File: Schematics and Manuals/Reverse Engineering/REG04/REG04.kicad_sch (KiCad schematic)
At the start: 203 parts, among them J1 Conn_01x02_Pin, J10 Conn_01x02_Pin, J11 Conn_01x02_Pin, J12 Conn_01x02_Pin, J13 Conn_01x02_Pin, J14 Conn_01x02_Pin, J15 Conn_01x02_Pin, J16 Conn_01x02_Pin, J17 Conn_01x02_Pin, J18 Conn_01x02_Pin, J19 Conn_01x02_Pin, J2 Conn_01x02_Pin, J20 Conn_01x02_Pin, J21 Conn_01x02_Pin, J22 Conn_01x02_Pin, J23 Conn_01x02_Pin, J24 Conn_01x02_Pin, J25 Conn_01x02_Pin, J26 Conn_01x02_Pin, J27 Conn_01x02_Pin, J28 Conn_01x02_Pin, J29 Conn_01x02_Pin, J3 Conn_01x02_Pin, J30 Conn_01x02_Pin, J31 Conn_01x02_Pin, J32 Conn_01x02_Pin, J33 Conn_01x02_Pin, J34 Conn_01x02_Pin, J35 Conn_01x02_Pin, J36 Conn_01x02_Pin, J37 Conn_01x02_Pin, J38 Conn_01x02_Pin, J39 Conn_01x02_Pin, J4 Conn_01x02_Pin, J40 Conn_01x02_Pin, J5 Conn_01x02_Pin, J6 Conn_01x02_Pin, J7 Conn_01x02_Pin, J8 Conn_01x02_Pin, J9 Conn_01x02_Pin, Q1 Q_PNP_EBC, Q10 Q_PNP_EBC, Q11 Q_PNP_EBC, Q12 Q_PNP_EBC, Q13 Q_PNP_EBC, Q14 Q_PNP_EBC, Q15 Q_PNP_EBC, Q16 Q_PNP_EBC, Q2 Q_PNP_EBC, Q3 Q_PNP_EBC, Q4 Q_PNP_EBC, Q5 Q_PNP_EBC, Q6 Q_PNP_EBC, Q7 Q_PNP_EBC, Q8 Q_PNP_EBC, Q9 Q_PNP_EBC

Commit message: Complete renumbering and reordering of the schematic and PCB
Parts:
- R46: renamed from R31; value R -> 10k
- R61: renamed from R16; value R -> 10k
- renumbered C22 to C1, C14 to C10, C15 to C11, C9 to C13, C10 to C14, C11 to C15, C8 to C16, C5 to C17, C6 to C18, C7 to C19, C21 to C2, C4 to C20, C2 to C21, C3 to C22, C1 to C23, C18 to C3, C20 to C4, C17 to C5, C19 to C6, C23 to C7, C16 to C8, C13 to C9, D43 to D1, D35 to D10, D46 to D11, D34 to D12, D40 to D13, D33 to D14, D38 to D15, D39 to D16, D30 to D17, D31 to D18, D32 to D19, D48 to D2, D27 to D20, D28 to D21, D26 to D22, D29 to D23, D25 to D24, D22 to D25, D23 to D26, D24 to D27, D19 to D28, D20 to D29, D42 to D3, D21 to D30, D18 to D31, D17 to D32, D14 to D33, D15 to D34, D16 to D35, D11 to D36, D12 to D37, D13 to D38, D10 to D39, D45 to D4, D9 to D40, D7 to D41, D8 to D42, D6 to D43, D5 to D44, D3 to D45, D2 to D46, D4 to D47, D1 to D48, D37 to D5, D36 to D6, D44 to D7, D41 to D8, D47 to D9, J40 to J1, J31 to J10, J30 to J11, J29 to J12, J28 to J13, J27 to J14, J26 to J15, J25 to J16, J24 to J17, J23 to J18, J22 to J19, J39 to J2, J21 to J20, J20 to J21, J19 to J22, J18 to J23, J17 to J24, J16 to J25, J15 to J26, J14 to J27, J13 to J28, J12 to J29, J38 to J3, J11 to J30, J10 to J31, J9 to J32, J8 to J33, J7 to J34, J6 to J35, J5 to J36, J4 to J37, J3 to J38, J2 to J39, J37 to J4, J1 to J40, J36 to J5, J35 to J6, J34 to J7, J33 to J8, J32 to J9, Q14 to Q1, Q8 to Q10, Q6 to Q11, Q4 to Q12, Q5 to Q13, Q2 to Q14, Q3 to Q15, Q1 to Q16, Q16 to Q2, Q15 to Q3, Q13 to Q4, Q12 to Q5, Q11 to Q6, Q10 to Q7, Q9 to Q8, Q7 to Q9, R71 to R1, R75 to R10, R65 to R11, R76 to R12, R64 to R13, R63 to R14, R62 to R15, R61 to R16, R59 to R17, R60 to R18, R55 to R19, R67 to R2, R57 to R20, R58 to R21, R54 to R22, R50 to R23, R52 to R24, R53 to R25, R49 to R26, R51 to R27, R46 to R28, R47 to R29, R68 to R3, R48 to R30, R56 to R31, R45 to R32, R44 to R33, R40 to R34, R42 to R35, R43 to R36, R39 to R37, R35 to R38, R37 to R39, R74 to R4, R38 to R40, R34 to R41, R32 to R42, R36 to R43, R33 to R44, R41 to R45, R30 to R47, R29 to R48, R25 to R49, R69 to R5, R27 to R50, R28 to R51, R20 to R52, R22 to R53, R23 to R54, R24 to R55, R17 to R56, R19 to R57, R21 to R58, R18 to R59, R70 to R6, R26 to R60, R7 to R62, R5 to R63, R11 to R64, R4 to R65, R13 to R66, R3 to R67, R10 to R68, R15 to R69, R66 to R7, R12 to R70, R2 to R71, R8 to R72, R1 to R73, R6 to R74, R9 to R75, R14 to R76, R72 to R8, R73 to R9
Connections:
- net -12V: now also R24.2, R39.2, R53.2; no longer R24.1, R39.1, R53.1
- net GND: no longer R59.2
- net at D25.2 (A), R34.1, R36.1: now also C12.1; no longer C12.2
- net at C18.2, D36.2 (A), R54.1: now also R53.1; no longer R53.2
- net at C10.2, D20.2 (A), R25.1: now also R24.1; no longer R24.2
- net at D2.1 (K), Q3.2 (B), R10.1: now also C4.2; no longer C4.1
- net at D10.1 (K), D2.2 (A), D9.1 (K)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: now also C4.1; no longer C4.2
- net at C14.2, D28.2 (A), R40.1: now also R39.1; no longer R39.2
- net P1 renamed P40-FF1-~{Q}EN
- net P12 renamed P29-FF2-~{S}
- net P14 renamed P27-FF3-~{Q}EN
- net P15 renamed P26-FF3-~{Q}Z
- net P16 Q3-CLK renamed P25-FF3-~{CLK}
- net P25-FF3-~{CLK}: now also C12.2; no longer C12.1
- net P18 renamed P23-FF3-~{S}
- net P19 renamed P22-FF4-~{Q}EN
- net P2 renamed P39-FF1-~{Q}Z
- net P20 renamed P21-FF4-~{Q}Z
- net P21 GRset renamed P20-BUS-~{RES}
- net P22 Q4-CLK renamed P19-FF4-~{CLK}
- net P24 renamed P17-FF4-~{S}
- net P26 Gset renamed P15-BUS-~{SET}
- net P27 renamed P14-FF3-Q
- net P29 Gout renamed P12-BUS-OUT
- net P3 Q1-CLK renamed P38-FF1-~{CLK}
- net P30 A renamed P11-FF5-SEN
- net P31 IO renamed P10-FF5-Q
- net P32 Out renamed P9-FF5-~{Q}
- net P33 B renamed P8-FF5-~{S}
- net P34 OutZ renamed P7-FF5-~{Q}Z
- net P35 C renamed P6-FF5-~{R}
- net P36 D renamed P5-FF5-~{REN2}
- net P37 E renamed P4-FF5-~{REN1}
- net P5 renamed P36-FF1-~{S}
- net P6 renamed P35-FF2-~{Q}EN
- net P7 renamed P34-FF2-~{Q}Z
- net P9 Q2-CLK renamed P32-FF2-~{CLK}
- net ~{Gout} renamed ~{BUS-OUT}
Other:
- note added: "Edits by Roy20100"
- note added: "Q1k"
- note added: "Q2k"
- note added: "Q3k"
- note added: "Q4k"
- note removed: "-1V"
- note removed: "Minor Edits by Roy20100"
- note removed: "Out=~{IO&C}&~{D&E} IO=~{Out&B}&A"
- note removed: "P32=~{P31&P35}&~{P36&P37} P31=~{P32&P33}&P30"
- moved on the sheet: C1, C10, C12, C14, C16, C18, C2, C20, C22, C3, C4, C5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

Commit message: Reformed Schematic to A3 size and removed bus lines
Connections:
- net GND: now also R59.2
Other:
- note added: "BUS"
- note added: "FF1"
- note added: "FF2"
- note added: "FF3"
- note added: "FF4"
- note added: "FF5"
- note removed: "A"
- note removed: "B"
- note removed: "C"
- note removed: "D"
- note removed: "E"
- note removed: "GOut"
- note removed: "GRset"
- note removed: "GSet"
- note removed: "IO"
- note removed: "Out"
- note removed: "OutZ"
- note removed: "Q1k"
- note removed: "Q2k"
- note removed: "Q3"
- note removed: "Q3k"
- note removed: "Q4k"
- note removed: "S1"
- note removed: "S2"
- note removed: "S3"
- note removed: "S4"
- note removed: "~{Q}1"
- note removed: "~{Q}1 en Gout"
- note removed: "~{Q}2"
- note removed: "~{Q}2 en Gout"
- note removed: "~{Q}3"
- note removed: "~{Q}3 en Gout"
- note removed: "~{Q}4"
- note removed: "~{Q}4 en Gout"
- moved on the sheet: C1, C10, C11, C12, C13, C14, C15, C16, C17, C18, C19, C2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

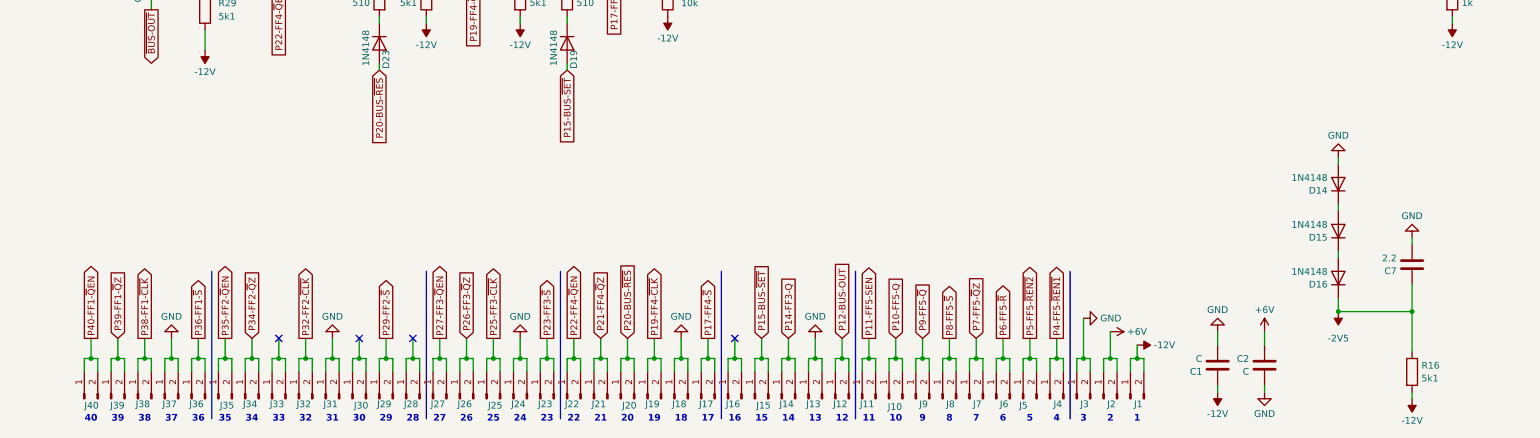
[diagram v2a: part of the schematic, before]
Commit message: Replaced connector for the standard connector and created a PCB part for the 40 pin ELCO like connector
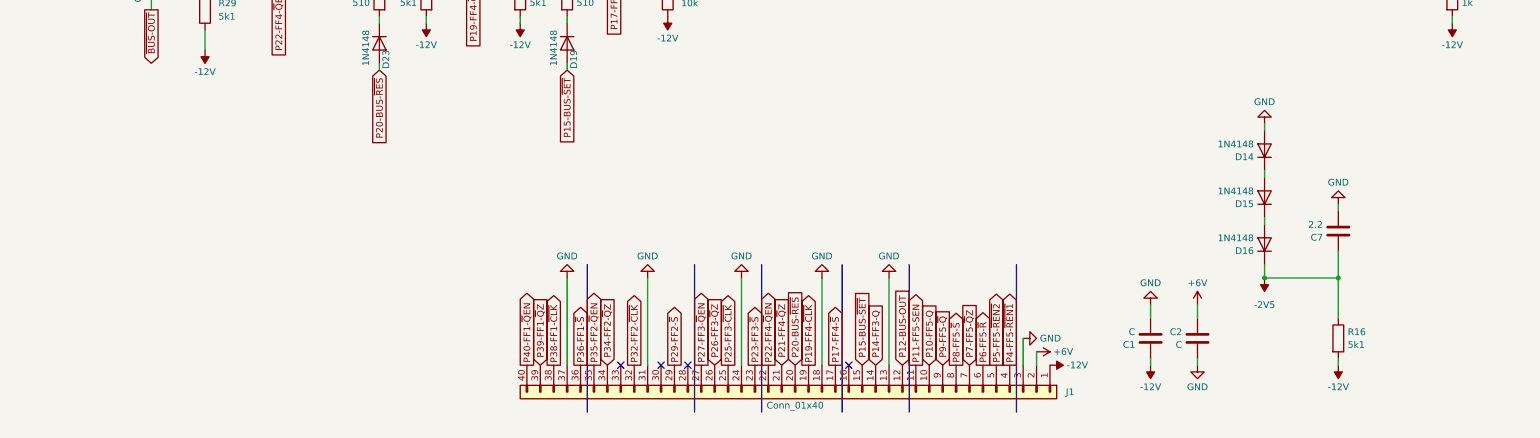
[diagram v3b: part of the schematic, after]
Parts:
- removed J1, J10, J11, J12, J13, J14, J15, J16, J17, J18, J19, J2, J20, J21, J22, J23, J24, J25, J26, J27, J28, J29, J3, J30, J31, J32, J33, J34, J35, J36, J37, J38, J39, J4, J40, J5, J6, J7, J8, J9: Conn_01x02_Pin, TestPoint:TestPoint_2Pads_Pitch5.08mm_Drill1.3mm, symbol Connector:Conn_01x02_Pin
- added J1: Conn_01x40, Logi620:ELCO 40, symbol Connector_Generic:Conn_01x40
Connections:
- net +6V: now also J1.2 (Pin_2)
- net -12V: now also J1.1 (Pin_1)
- net GND: now also J1.13 (Pin_13), J1.18 (Pin_18), J1.24 (Pin_24), J1.3 (Pin_3), J1.31 (Pin_31), J1.37 (Pin_37)
- net P10-FF5-Q: now also J1.10 (Pin_10)
- net P11-FF5-SEN: now also J1.11 (Pin_11)
- net P12-BUS-OUT: now also J1.12 (Pin_12)
- net P14-FF3-Q: now also J1.14 (Pin_14)
- net P15-BUS-~{SET}: now also J1.15 (Pin_15)
- net P17-FF4-~{S}: now also J1.17 (Pin_17)
- net P19-FF4-~{CLK}: now also J1.19 (Pin_19)
- net P20-BUS-~{RES}: now also J1.20 (Pin_20)
- net P21-FF4-~{Q}Z: now also J1.21 (Pin_21)
- net P22-FF4-~{Q}EN: now also J1.22 (Pin_22)
- net P23-FF3-~{S}: now also J1.23 (Pin_23)
- net P25-FF3-~{CLK}: now also J1.25 (Pin_25)
- net P26-FF3-~{Q}Z: now also J1.26 (Pin_26)
- net P27-FF3-~{Q}EN: now also J1.27 (Pin_27)
- net P29-FF2-~{S}: now also J1.29 (Pin_29)
- net P32-FF2-~{CLK}: now also J1.32 (Pin_32)
- net P34-FF2-~{Q}Z: now also J1.34 (Pin_34)
- net P35-FF2-~{Q}EN: now also J1.35 (Pin_35)
- net P36-FF1-~{S}: now also J1.36 (Pin_36)
- net P38-FF1-~{CLK}: now also J1.38 (Pin_38)
- net P39-FF1-~{Q}Z: now also J1.39 (Pin_39)
- net P4-FF5-~{REN1}: now also J1.4 (Pin_4)
- net P40-FF1-~{Q}EN: now also J1.40 (Pin_40)
- net P5-FF5-~{REN2}: now also J1.5 (Pin_5)
- net P6-FF5-~{R}: now also J1.6 (Pin_6)
- net P7-FF5-~{Q}Z: now also J1.7 (Pin_7)
- net P8-FF5-~{S}: now also J1.8 (Pin_8)
- net P9-FF5-~{Q}: now also J1.9 (Pin_9)
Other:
- note removed: "1"
- note removed: "10"
- note removed: "11"
- note removed: "12"
- note removed: "13"
- note removed: "14"
- note removed: "15"
- note removed: "16"
- note removed: "17"
- note removed: "18"
- note removed: "19"
- note removed: "2"
- note removed: "20"
- note removed: "21"
- note removed: "22"
- note removed: "23"
- note removed: "24"
- note removed: "25"
- note removed: "26"
- note removed: "27"
- note removed: "28"
- note removed: "29"
- note removed: "3"
- note removed: "30"
- note removed: "31"
- note removed: "32"
- note removed: "33"
- note removed: "34"
- note removed: "35"
- note removed: "36"
- note removed: "37"
- note removed: "38"
- note removed: "39"
- note removed: "4"
- note removed: "40"
- note removed: "5"
- note removed: "6"
- note removed: "7"
- note removed: "8"
- note removed: "9"
- moved on the sheet: C1, C2, C7, D14, D15, D16, R16
